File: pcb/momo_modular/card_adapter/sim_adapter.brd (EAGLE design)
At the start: 100 x 80 mm, 6 parts, among them U1 ESDA6V1SC6

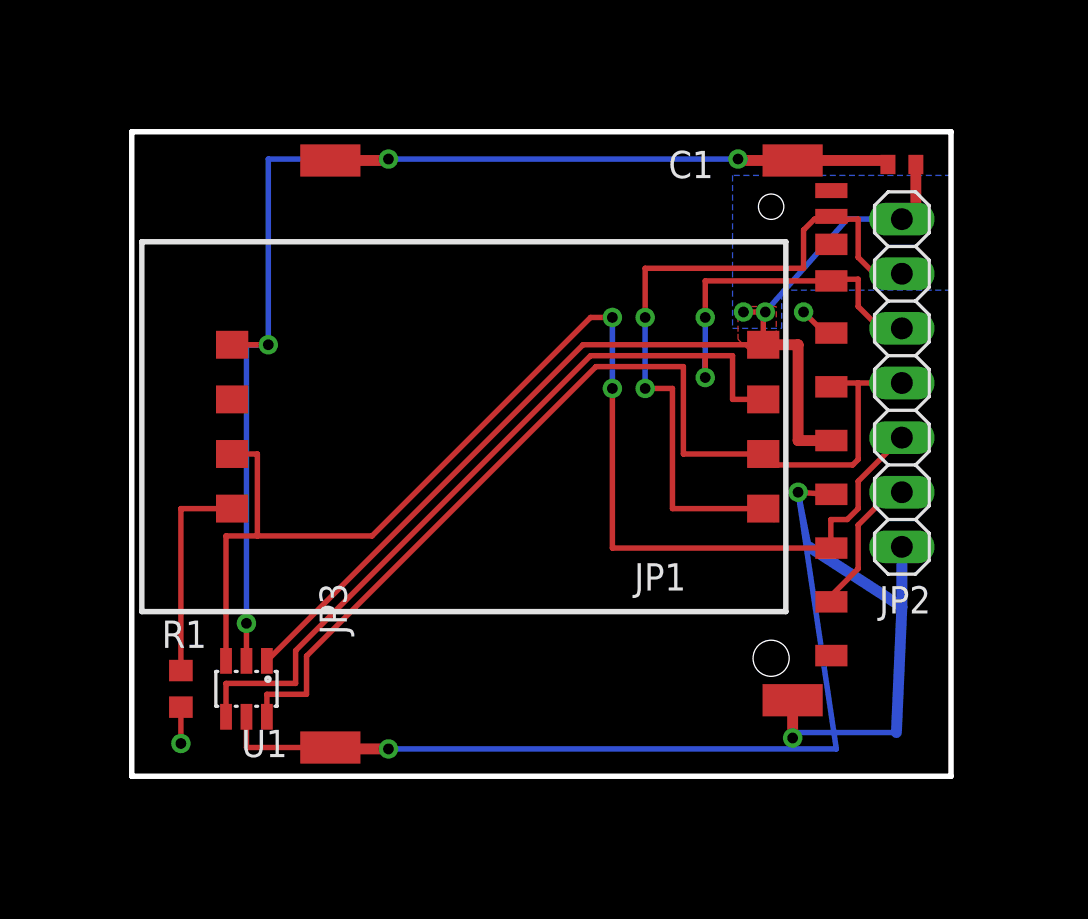
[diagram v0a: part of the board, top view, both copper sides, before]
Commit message: Finalize sd/sim card adapter board
- make size a round number
- make pinout standard for minimal wiring
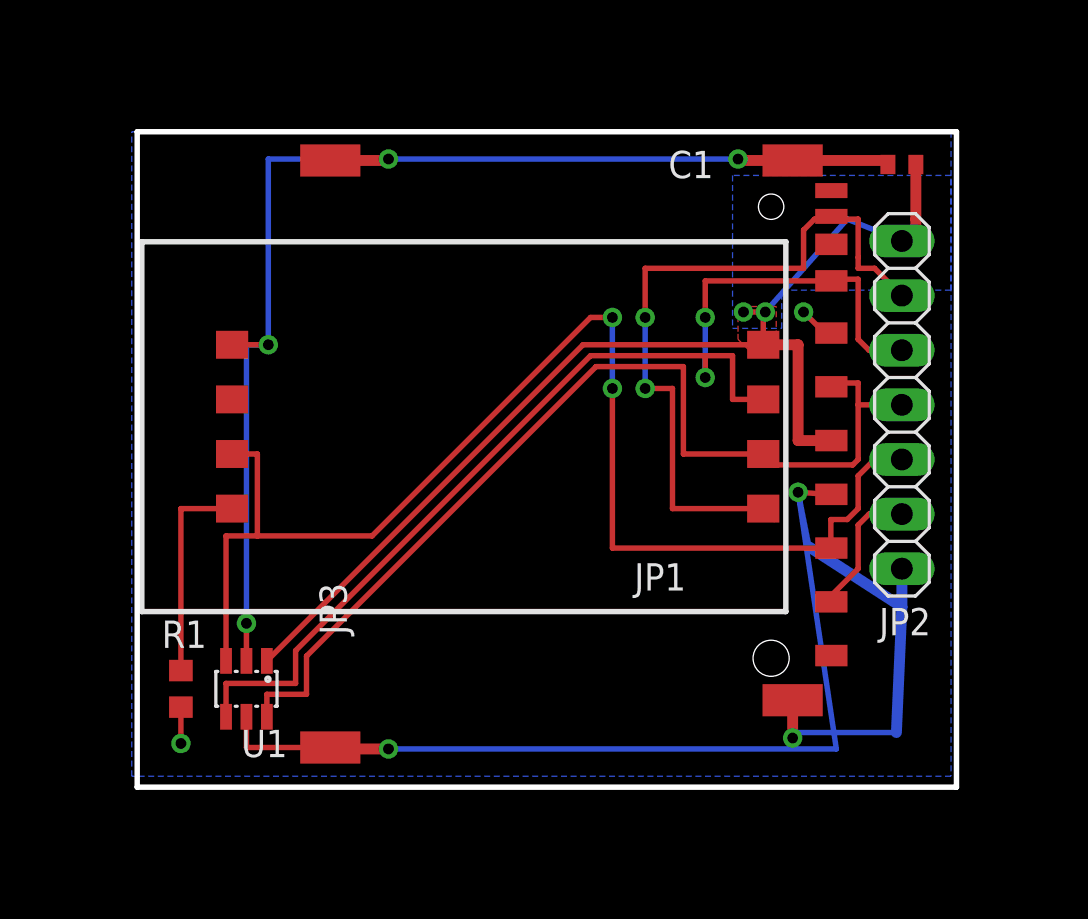
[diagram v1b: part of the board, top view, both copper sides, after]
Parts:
- moved JP2 1.02 mm to (56.1, 41.1)
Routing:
- net IO3: track 52.2 -> 53.5 mm
- net GND: track 126.9 -> 125.9 mm
- net VCC: track 50.9 -> 51.7 mm
- net SENSE: track 33.5 -> 34.2 mm
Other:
- outline, holes or cut-outs redrawn
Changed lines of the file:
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@@
 <?xml version="1.0" encoding="utf-8"?>
 <!DOCTYPE eagle SYSTEM "eagle.dtd">
-<eagle version="6.5.0">
+<eagle version="6.4">
 <drawing>
 <settings>
@@
 <wire x1="100" y1="80" x2="0" y2="80" width="0" layer="20"/>
 <wire x1="0" y1="80" x2="0" y2="0" width="0" layer="20"/>
-<wire x1="58.42" y1="53.848" x2="58.42" y2="23.876" width="0.254" layer="20"/>
-<wire x1="58.42" y1="23.876" x2="20.32" y2="23.876" width="0.254" layer="20"/>
-<wire x1="20.32" y1="23.876" x2="20.32" y2="53.848" width="0.254" layer="20"/>
-<wire x1="20.32" y1="53.848" x2="58.42" y2="53.848" width="0.254" layer="20"/>
-<dimension x1="20.32" y1="53.848" x2="58.42" y2="53.848" x3="39.37" y3="56.388" textsize="1.778" layer="49" dtype="horizontal" unit="inch" precision="3" visible="yes"/>
-<dimension x1="20.32" y1="53.848" x2="20.32" y2="23.876" x3="18.542" y3="38.862" textsize="1.778" layer="49" dtype="vertical" unit="inch" precision="3" visible="yes"/>
+<wire x1="58.674" y1="53.848" x2="58.674" y2="23.368" width="0.254" layer="20"/>
+<wire x1="58.674" y1="23.368" x2="20.574" y2="23.368" width="0.254" layer="20"/>
+<wire x1="20.574" y1="23.368" x2="20.574" y2="53.848" width="0.254" layer="20"/>
+<wire x1="20.574" y1="53.848" x2="58.674" y2="53.848" width="0.254" layer="20"/>
+<dimension x1="56.134" y1="41.148" x2="58.42" y2="53.848" x3="62.23" y3="47.498" textsize="1.778" layer="49" dtype="vertical" unit="inch" precision="3" visible="yes"/>
+<dimension x1="20.32" y1="53.848" x2="20.32" y2="23.368" x3="17.526" y3="38.608" textsize="1.778" layer="49" dtype="vertical" unit="inch" precision="3" visible="yes"/>
+<dimension x1="20.574" y1="53.848" x2="58.674" y2="53.848" x3="39.624" y3="56.642" textsize="1.778" layer="49" dtype="horizontal" unit="inch" precision="3" visible="yes"/>
+<dimension x1="56.134" y1="41.148" x2="58.674" y2="23.368" x3="57.404" y3="20.828" textsize="1.778" layer="49" dtype="horizontal" unit="inch" precision="3" visible="yes"/>
 </plain>
 <attributes>
@@
 <attribute name="DIGIKEY-PN-SIM" x="51.054" y="38.862" size="1.778" layer="27" rot="R270" display="off"/>
 </element>
-<element name="JP2" library="pinhead" package="1X07" value="" x="56.134" y="42.164" smashed="yes" rot="R90">
-<attribute name="NAME" x="57.4802" y="32.7152" size="1.27" layer="25" ratio="10" rot="R180"/>
-<attribute name="VALUE" x="59.309" y="33.274" size="1.27" layer="27" rot="R90"/>
+<element name="JP2" library="pinhead" package="1X07" value="" x="56.134" y="41.148" smashed="yes" rot="R90">
+<attribute name="NAME" x="57.4802" y="31.6992" size="1.27" layer="25" ratio="10" rot="R180"/>
+<attribute name="VALUE" x="59.309" y="32.258" size="1.27" layer="27" rot="R90"/>
 </element>
 </elements>
@@
 <wire x1="49.688" y1="45.37" x2="49.784" y2="45.466" width="0.254" layer="1"/>
 <wire x1="49.784" y1="45.466" x2="48.768" y2="45.466" width="0.254" layer="1"/>
-<wire x1="56.134" y1="49.784" x2="53.594" y2="49.784" width="0.254" layer="16"/>
+<wire x1="56.134" y1="48.768" x2="53.594" y2="49.784" width="0.254" layer="16"/>
 <wire x1="53.594" y1="49.784" x2="49.784" y2="45.466" width="0.254" layer="16"/>
-<wire x1="56.134" y1="49.784" x2="56.784" y2="49.784" width="0.508" layer="1"/>
 <wire x1="56.784" y1="49.784" x2="56.784" y2="52.324" width="0.508" layer="1"/>
 <polygon width="0.254" layer="16" isolate="0.254">
@@
 <vertex x="49.022" y="43.434"/>
 </polygon>
+<wire x1="56.784" y1="49.784" x2="56.784" y2="49.418" width="0.508" layer="1"/>
+<wire x1="56.784" y1="49.418" x2="56.134" y2="48.768" width="0.508" layer="1"/>
 </signal>
 <signal name="GND">
@@
 <wire x1="52.854" y1="44.487" x2="52.541" y2="44.487" width="0.254" layer="1"/>
 <wire x1="52.541" y1="44.487" x2="51.562" y2="45.466" width="0.254" layer="1"/>
-<wire x1="56.134" y1="34.544" x2="56.134" y2="31.75" width="0.508" layer="16"/>
+<wire x1="56.134" y1="33.528" x2="56.134" y2="31.75" width="0.508" layer="16"/>
 <wire x1="56.134" y1="31.75" x2="55.88" y2="25.908" width="0.508" layer="16"/>
 <wire x1="55.88" y1="25.908" x2="51.054" y2="25.908" width="0.254" layer="16"/>
@@
 <wire x1="52.854" y1="32.28" x2="54.102" y2="33.528" width="0.254" layer="1"/>
 <wire x1="54.102" y1="33.528" x2="54.102" y2="35.56" width="0.254" layer="1"/>
-<wire x1="54.102" y1="35.56" x2="55.626" y2="37.084" width="0.254" layer="1"/>
-<wire x1="55.626" y1="37.084" x2="56.134" y2="37.084" width="0.254" layer="1"/>
+<wire x1="54.102" y1="35.56" x2="54.61" y2="36.068" width="0.254" layer="1"/>
+<wire x1="54.61" y1="36.068" x2="56.134" y2="36.068" width="0.254" layer="1"/>
 </signal>
 <signal name="IO2">
@@
 <wire x1="24.704" y1="35.052" x2="24.704" y2="29.24" width="0.254" layer="1"/>
 <contactref element="JP2" pad="3"/>
-<wire x1="56.134" y1="39.624" x2="54.102" y2="37.592" width="0.254" layer="1"/>
 <wire x1="53.029" y1="34.487" x2="52.854" y2="34.487" width="0.254" layer="1"/>
-<wire x1="54.102" y1="37.592" x2="54.102" y2="36.322" width="0.254" layer="1"/>
+<wire x1="54.102" y1="37.846" x2="54.102" y2="36.322" width="0.254" layer="1"/>
 <wire x1="54.102" y1="36.322" x2="53.594" y2="35.814" width="0.254" layer="1"/>
 <wire x1="53.594" y1="35.814" x2="52.832" y2="35.814" width="0.254" layer="1"/>
@@
 <wire x1="42.672" y1="41.91" x2="42.672" y2="34.487" width="0.254" layer="1"/>
 <wire x1="42.672" y1="34.487" x2="52.854" y2="34.487" width="0.254" layer="1"/>
+<wire x1="54.102" y1="37.846" x2="54.864" y2="38.608" width="0.254" layer="1"/>
+<wire x1="54.864" y1="38.608" x2="56.134" y2="38.608" width="0.254" layer="1"/>
 </signal>
 <signal name="IO3">
@@
 <via x="46.99" y="42.418" extent="1-16" drill="0.5"/>
 <wire x1="46.99" y1="42.418" x2="46.99" y2="43.434" width="0.254" layer="1"/>
-<wire x1="54.102" y1="46.99" x2="52.854" y2="46.99" width="0.254" layer="1"/>
 <wire x1="52.854" y1="46.99" x2="52.854" y2="46.912" width="0.254" layer="1"/>
 <contactref element="JP2" pad="5"/>
-<wire x1="56.134" y1="44.704" x2="55.118" y2="44.704" width="0.254" layer="1"/>
-<wire x1="55.118" y1="44.704" x2="54.102" y2="45.72" width="0.254" layer="1"/>
-<wire x1="54.102" y1="45.72" x2="54.102" y2="46.99" width="0.254" layer="1"/>
+<wire x1="56.134" y1="43.688" x2="54.61" y2="43.688" width="0.254" layer="1"/>
+<wire x1="54.61" y1="43.688" x2="54.102" y2="44.196" width="0.254" layer="1"/>
+<wire x1="54.102" y1="44.196" x2="54.102" y2="46.99" width="0.254" layer="1"/>
+<wire x1="54.102" y1="46.99" x2="52.932" y2="46.99" width="0.254" layer="1"/>
+<wire x1="52.932" y1="46.99" x2="52.854" y2="46.912" width="0.254" layer="1"/>
 </signal>
 <signal name="IO4">
@@
 <wire x1="49.688" y1="38.862" x2="49.942" y2="38.608" width="0.254" layer="1"/>
 <contactref element="JP2" pad="4"/>
-<wire x1="56.134" y1="42.164" x2="54.102" y2="42.164" width="0.254" layer="1"/>
 <wire x1="54.102" y1="42.164" x2="53.031" y2="42.164" width="0.254" layer="1"/>
 <wire x1="53.031" y1="42.164" x2="52.854" y2="41.987" width="0.254" layer="1"/>
@@
 <wire x1="50.196" y1="38.354" x2="53.848" y2="38.354" width="0.254" layer="1"/>
 <wire x1="53.848" y1="38.354" x2="54.102" y2="38.608" width="0.254" layer="1"/>
-<wire x1="54.102" y1="38.608" x2="54.102" y2="42.164" width="0.254" layer="1"/>
+<wire x1="54.102" y1="38.608" x2="54.102" y2="41.148" width="0.254" layer="1"/>
+<wire x1="54.102" y1="41.148" x2="54.102" y2="42.164" width="0.254" layer="1"/>
+<wire x1="56.134" y1="41.148" x2="54.102" y2="41.148" width="0.254" layer="1"/>
 </signal>
 <signal name="SENSE">
@@
 <wire x1="52.726" y1="49.784" x2="52.854" y2="49.912" width="0.254" layer="1"/>
 <contactref element="JP2" pad="6"/>
-<wire x1="56.134" y1="47.244" x2="54.864" y2="47.244" width="0.254" layer="1"/>
-<wire x1="54.864" y1="47.244" x2="54.102" y2="48.006" width="0.254" layer="1"/>
 <wire x1="54.102" y1="48.006" x2="54.102" y2="49.784" width="0.254" layer="1"/>
 <wire x1="54.102" y1="49.784" x2="52.982" y2="49.784" width="0.254" layer="1"/>
 <wire x1="52.982" y1="49.784" x2="52.854" y2="49.912" width="0.254" layer="1"/>
+<wire x1="56.134" y1="46.228" x2="54.864" y2="47.498" width="0.254" layer="1"/>
+<wire x1="54.864" y1="47.498" x2="54.102" y2="47.498" width="0.254" layer="1"/>
+<wire x1="54.102" y1="47.498" x2="54.102" y2="48.006" width="0.254" layer="1"/>
 </signal>
 </signals>

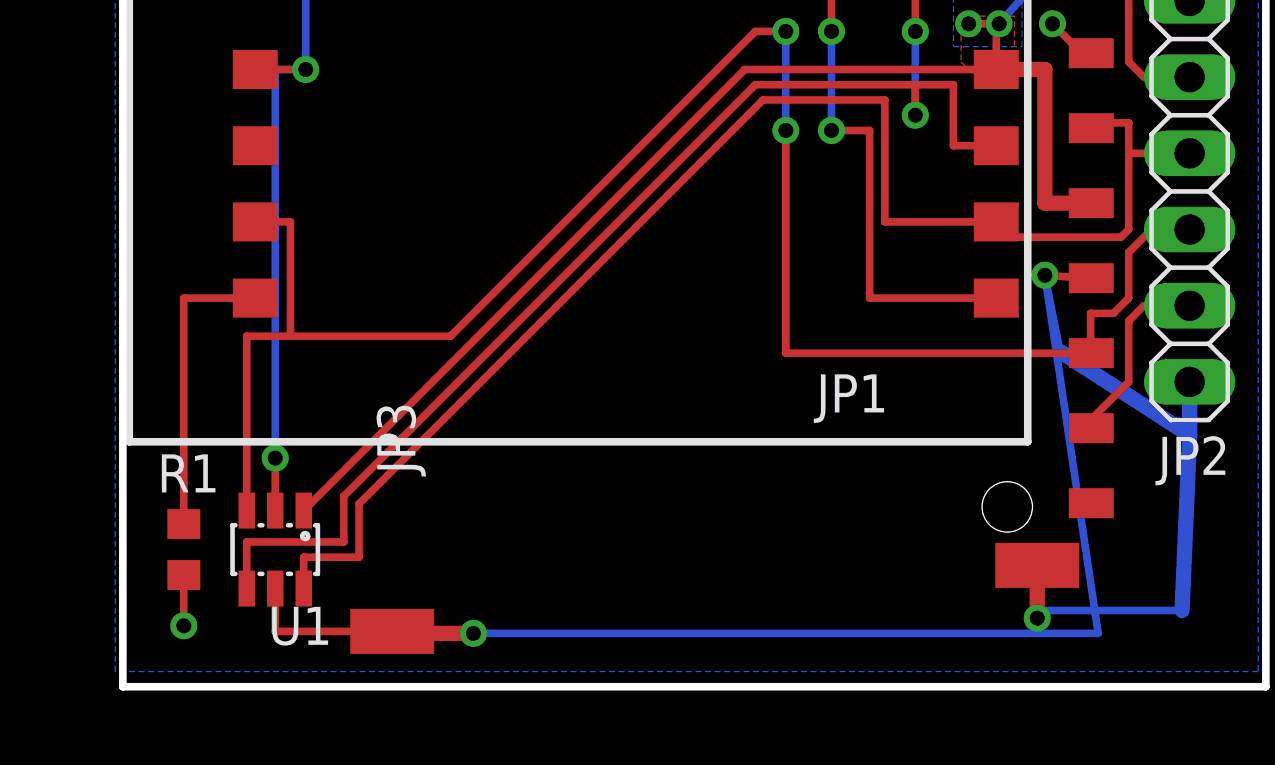
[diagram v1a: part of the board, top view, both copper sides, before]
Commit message: Add final wire for sensing sim insertion
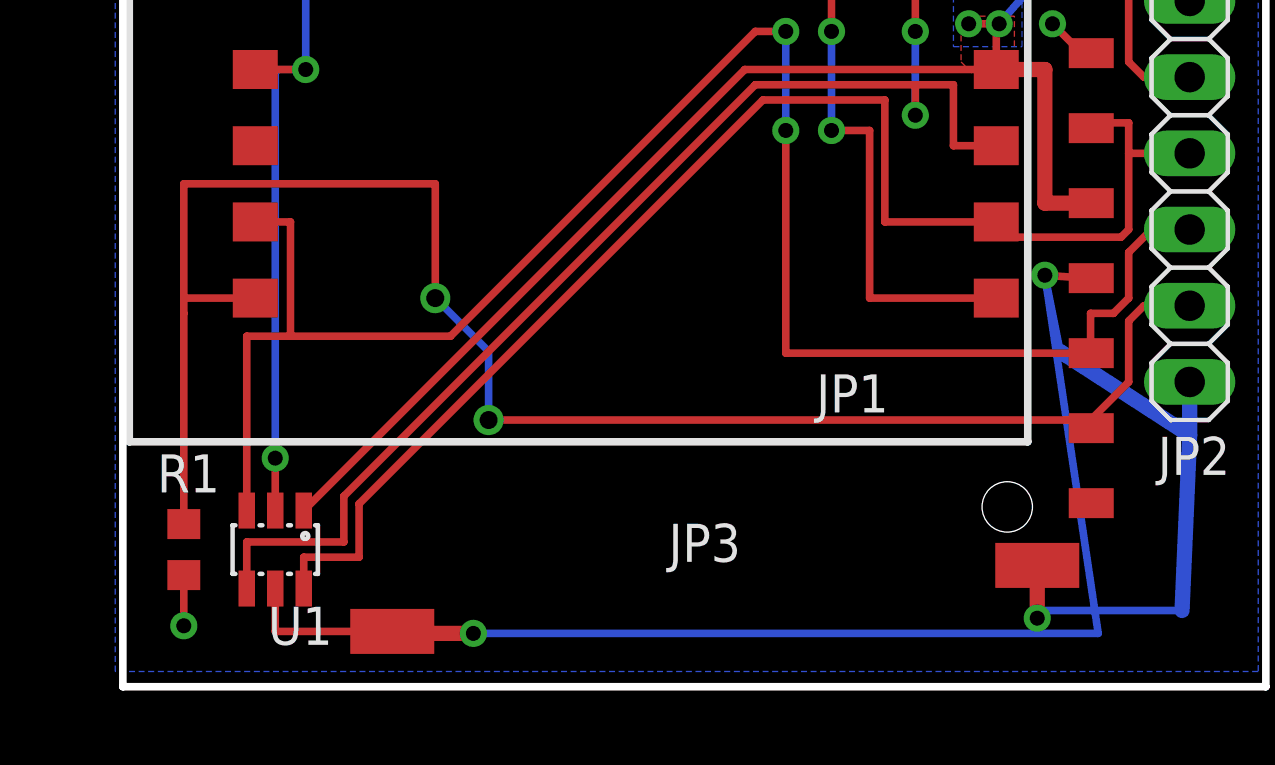
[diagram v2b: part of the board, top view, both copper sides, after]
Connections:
- removed net N$1: JP1.SW2, R1.1
- net IO1: now also JP1.SW2, R1.1
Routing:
- net IO1: track 6.33 -> 57.1 mm, vias 0 -> 2
- net N$1: track 9.91 -> 0.00 mm
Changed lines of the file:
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@@
 <?xml version="1.0" encoding="utf-8"?>
 <!DOCTYPE eagle SYSTEM "eagle.dtd">
-<eagle version="6.4">
+<eagle version="6.5.0">
 <drawing>
 <settings>
@@
 </plain>
 <attributes>
-<attribute name="HEIGHT" value="1.18"/>
+<attribute name="HEIGHT" value="1.2"/>
 <attribute name="PARTNAME" value="Card Adapter"/>
 <attribute name="REVISION" value="1"/>
@@
 <attribute name="NAME" x="21.717" y="29.845" size="1.27" layer="25"/>
 <attribute name="VALUE" x="20.701" y="28.575" size="1.27" layer="27" rot="R270"/>
+<attribute name="DIGIKEY-PN" value="P10.0KHCT-ND" x="22.606" y="27.94" size="1.778" layer="27" rot="R270" display="off"/>
 </element>
 <element name="C1" library="rcl" package="C0402" value="100 nF" x="56.134" y="52.324" smashed="yes" rot="R180">
 <attribute name="NAME" x="47.371" y="52.959" size="1.27" layer="25" rot="R180"/>
 <attribute name="VALUE" x="56.769" y="54.229" size="1.27" layer="27" rot="R180"/>
-</element>
-<element name="JP3" library="components" package="SDHOLDER-9PIN" value="SDCARD-HOLDER" x="51.054" y="38.862" rot="R270">
+<attribute name="DIGIKEY-PN" value="445-1265-1-ND" x="56.134" y="52.324" size="1.778" layer="27" rot="R180" display="off"/>
+</element>
+<element name="JP3" library="components" package="SDHOLDER-9PIN" value="SDCARD-HOLDER" x="51.054" y="38.862" smashed="yes" rot="R270">
 <attribute name="DIGIKEY-PN" value="732-3817-1-ND" x="51.054" y="38.862" size="1.778" layer="27" rot="R270" display="off"/>
-<attribute name="DIGIKEY-PN-SIM" x="51.054" y="38.862" size="1.778" layer="27" rot="R270" display="off"/>
+<attribute name="NAME" x="38.766" y="27.53" size="1.27" layer="25"/>
+<attribute name="POPULATE-SIM" value="no" x="51.054" y="38.862" size="1.778" layer="27" rot="R270" display="off"/>
 </element>
 <element name="JP2" library="pinhead" package="1X07" value="" x="56.134" y="41.148" smashed="yes" rot="R90">
 <attribute name="NAME" x="57.4802" y="31.6992" size="1.27" layer="25" ratio="10" rot="R180"/>
 <attribute name="VALUE" x="59.309" y="32.258" size="1.27" layer="27" rot="R90"/>
+<attribute name="POPULATE" value="no" x="56.134" y="41.148" size="1.778" layer="27" rot="R90" display="off"/>
 </element>
 </elements>
@@
 </polygon>
 </signal>
-<signal name="N$1">
-<contactref element="JP1" pad="SW2"/>
-<contactref element="R1" pad="1"/>
-<wire x1="22.606" y1="28.79" x2="22.606" y2="36.322" width="0.254" layer="1"/>
-<wire x1="22.606" y1="36.322" x2="24.988" y2="36.322" width="0.254" layer="1"/>
-</signal>
 <signal name="IO1">
 <contactref element="JP3" pad="1"/>
 <contactref element="JP2" pad="2"/>
-<wire x1="52.854" y1="31.987" x2="52.854" y2="32.28" width="0.254" layer="1"/>
+<wire x1="52.854" y1="31.987" x2="52.854" y2="32.258" width="0.254" layer="1"/>
 <wire x1="52.854" y1="32.28" x2="54.102" y2="33.528" width="0.254" layer="1"/>
 <wire x1="54.102" y1="33.528" x2="54.102" y2="35.56" width="0.254" layer="1"/>
 <wire x1="54.102" y1="35.56" x2="54.61" y2="36.068" width="0.254" layer="1"/>
 <wire x1="54.61" y1="36.068" x2="56.134" y2="36.068" width="0.254" layer="1"/>
+<contactref element="JP1" pad="SW2"/>
+<contactref element="R1" pad="1"/>
+<wire x1="22.606" y1="28.79" x2="22.606" y2="35.814" width="0.254" layer="1"/>
+<wire x1="22.606" y1="35.814" x2="22.606" y2="36.322" width="0.254" layer="1"/>
+<wire x1="22.606" y1="36.322" x2="24.988" y2="36.322" width="0.254" layer="1"/>
+<wire x1="52.854" y1="32.28" x2="52.854" y2="32.258" width="0.254" layer="1"/>
+<wire x1="52.854" y1="32.258" x2="32.766" y2="32.258" width="0.254" layer="1"/>
+<via x="32.766" y="32.258" extent="1-16" drill="0.6"/>
+<wire x1="32.766" y1="32.258" x2="32.766" y2="34.544" width="0.254" layer="16"/>
+<wire x1="32.766" y1="34.544" x2="30.988" y2="36.322" width="0.254" layer="16"/>
+<via x="30.988" y="36.322" extent="1-16" drill="0.6"/>
+<wire x1="30.988" y1="36.322" x2="30.988" y2="40.132" width="0.254" layer="1"/>
+<wire x1="30.988" y1="40.132" x2="22.606" y2="40.132" width="0.254" layer="1"/>
+<wire x1="22.606" y1="40.132" x2="22.606" y2="36.322" width="0.254" layer="1"/>
 </signal>
 <signal name="IO2">
